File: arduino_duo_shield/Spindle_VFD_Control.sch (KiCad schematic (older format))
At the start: 27 parts, among them K2 JQC-3F, K3 JQC-3F, Q3 2N7000, Q4 BS250, Q5 2N7000, Q6 2N7000, U3 LM358, U7 PC817, U8 PC817, U9 PC817

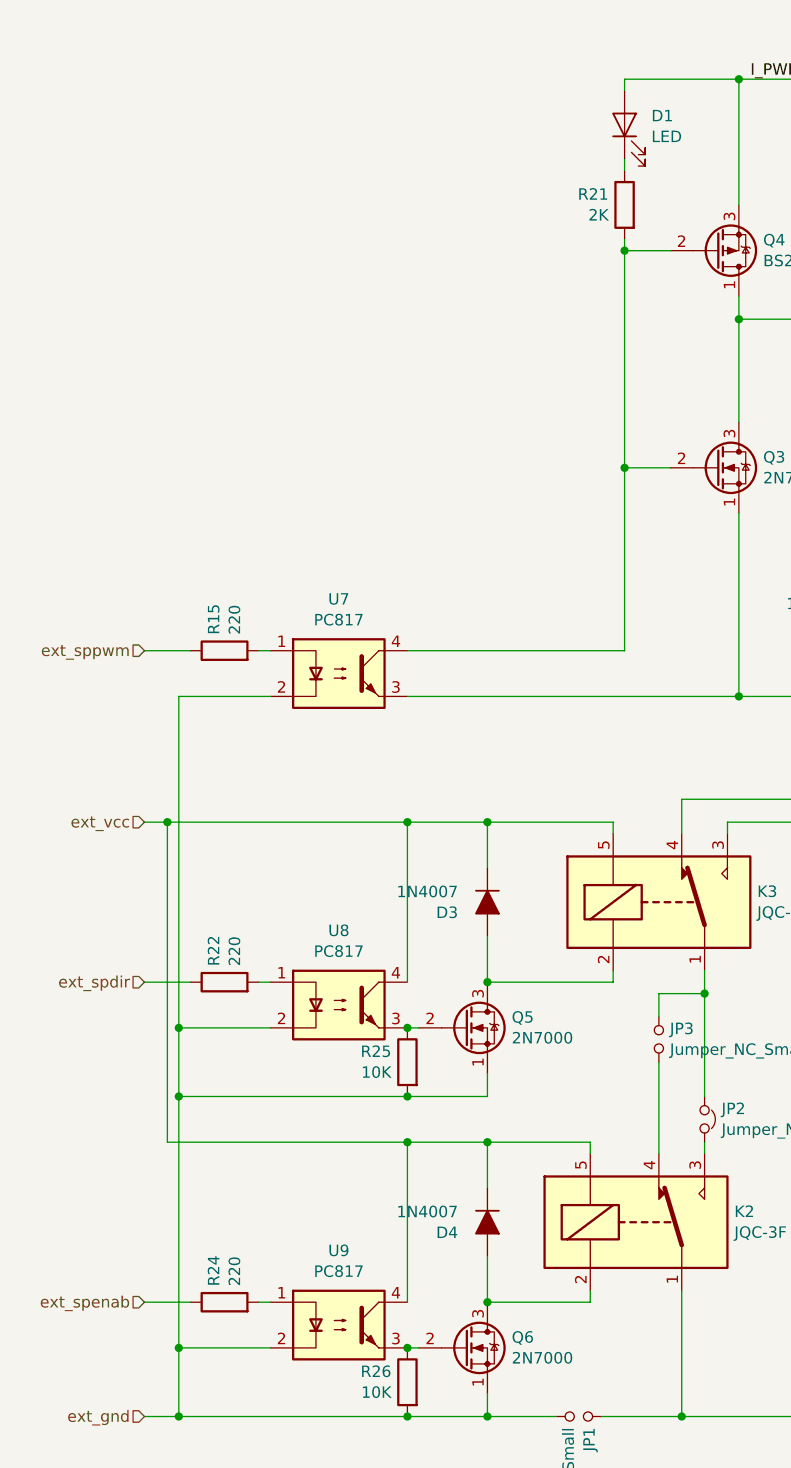
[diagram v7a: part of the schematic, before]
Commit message: Add support for spindle estop
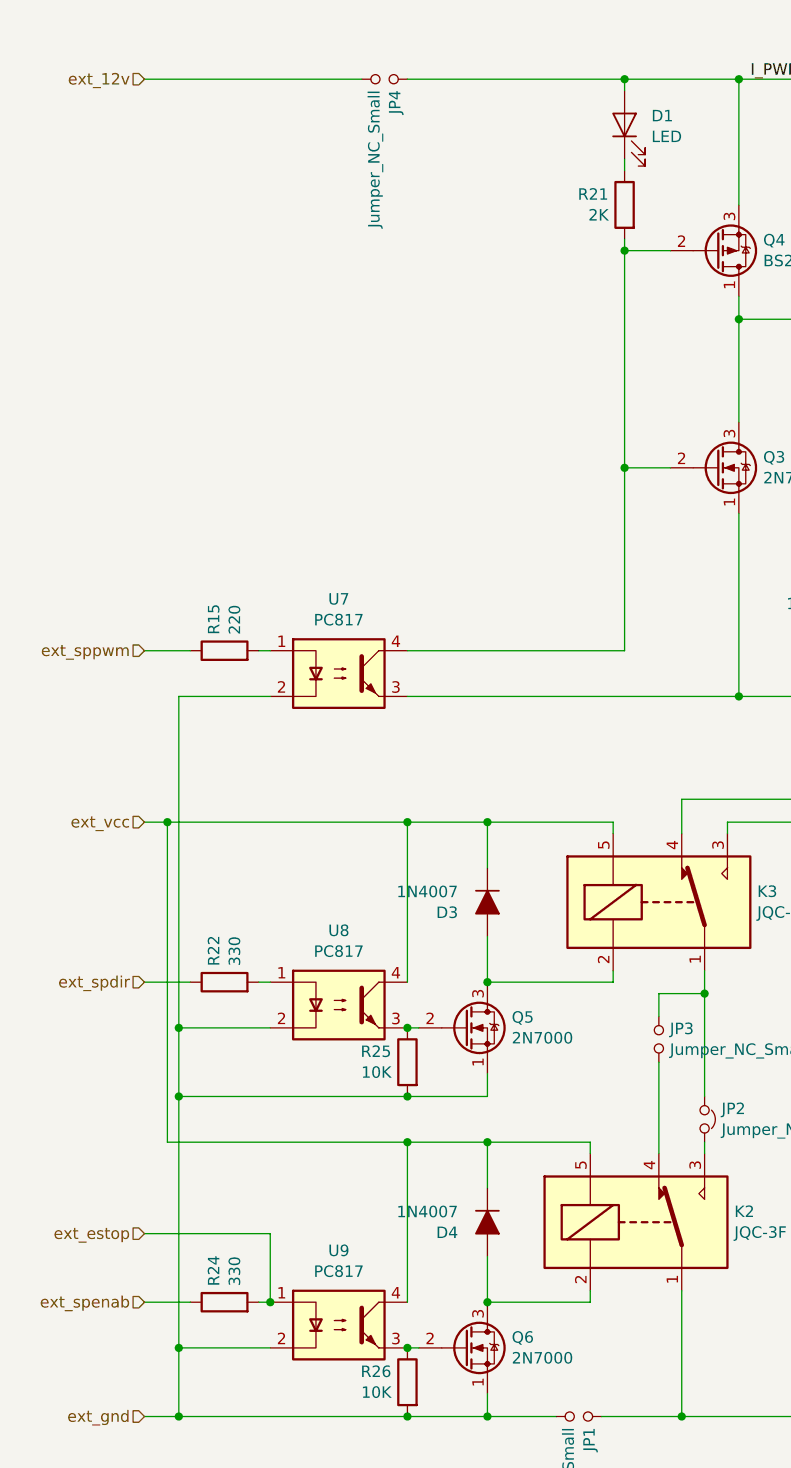
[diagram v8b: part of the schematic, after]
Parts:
- added JP4: Jumper_NC_Small, Connector_PinHeader_2.54mm:PinHeader_1x02_P2.54mm_Vertical, symbol Device:Jumper_NO_Small
- R22, R24: value 220 -> 330
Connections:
- net I_PWRSAFE: now also JP4.1
- net ext_estop: now reaches R24.2, U9.1
- new net ext_12v: JP4.2
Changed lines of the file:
@@
 AR Path="/5DD17641/5DE4EF5E" Ref="R22"  Part="1"
 F 0 "R22" H 1870 5096 50  0000 L CNN
-F 1 "220" H 1870 5005 50  0000 L CNN
+F 1 "330" H 1870 5005 50  0000 L CNN
 F 2 "Resistor_THT:R_Axial_DIN0207_L6.3mm_D2.5mm_P7.62mm_Horizontal" V 1730 5050 50  0001 C CNN
 F 3 "~" H 1800 5050 50  0001 C CNN
@@
 AR Path="/5DD17641/5DE55540" Ref="R24"  Part="1"
 F 0 "R24" H 1870 6496 50  0000 L CNN
-F 1 "220" H 1870 6405 50  0000 L CNN
+F 1 "330" H 1870 6405 50  0000 L CNN
 F 2 "Resistor_THT:R_Axial_DIN0207_L6.3mm_D2.5mm_P7.62mm_Horizontal" V 1730 6450 50  0001 C CNN
 F 3 "~" H 1800 6450 50  0001 C CNN
@@
 	5200 2950 6050 2950
 Connection ~ 5200 2950
+Text HLabel 1450 1100 0    50   Input ~ 0
+ext_12v
+Wire Wire Line
+	3550 1100 2600 1100
+Connection ~ 3550 1100
+$Comp
+L Device:Jumper_NO_Small JP4
+U 1 1 5E2A8878
+P 2500 1100
+F 0 "JP4" V 2454 1148 50  0000 L CNN
+F 1 "Jumper_NC_Small" V 2545 1148 50  0000 L CNN
+F 2 "Connector_PinHeader_2.54mm:PinHeader_1x02_P2.54mm_Vertical" H 2500 1100 50  0001 C CNN
+F 3 "~" H 2500 1100 50  0001 C CNN
+	1    2500 1100
+	-1   0    0    1
+$EndComp
+Wire Wire Line
+	2400 1100 1450 1100
+Text HLabel 1450 6150 0    50   Input ~ 0
+ext_estop
+Wire Wire Line
+	1450 6150 2000 6150
+Wire Wire Line
+	2000 6150 2000 6450
+Connection ~ 2000 6450
 $EndSCHEMATC
